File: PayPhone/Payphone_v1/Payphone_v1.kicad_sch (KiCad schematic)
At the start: 0 parts

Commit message: Payphone_v1: schematic started (MCP23008, relay, J1, U2 placed)
Co-Authored-By: Claude Sonnet 5.5 <noreply@anthropic.com>
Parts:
- added J1: JST_05, Connector_JST:JST_EH_B5B-EH-A_1x05_P2.50mm_Vertical, symbol PCM_SL_Connectors:JST_05
- added K1: G6S-2, symbol Relay:G6S-2
- added U1: MCP23008-xP, Package_DIP:DIP-18_W7.62mm, symbol Interface_Expansion:MCP23008-xP
- added U2: MC34063AP, Package_DIP:DIP-8_W7.62mm, symbol Regulator_Switching:MC34063AP

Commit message: Payphone_v1: all active parts, diodes, C_out, inductors, trimmer and connectors placed with footprints (no wires)
Co-Authored-By: Claude Sonnet 5.5 <noreply@anthropic.com>
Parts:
- added C1: 220uF/200V, Capacitor_THT:CP_Radial_D18.0mm_P7.50mm, symbol Device:C_Polarized
- added D1: 1N5819, Diode_THT:D_DO-41_SOD81_P10.16mm_Horizontal, symbol Diode:1N5819
- added D2: UF4003, Diode_THT:D_DO-41_SOD81_P10.16mm_Horizontal, symbol Custom:UF4003
- added D3: 1.5KE150A, Diode_THT:D_DO-201AD_P15.24mm_Horizontal, symbol Diode:1.5KExxA
- added D4: 1N4148, Diode_THT:D_DO-35_SOD27_P7.62mm_Horizontal, symbol Diode:1N4148
- added D5: 15V, Diode_THT:D_DO-41_SOD81_P10.16mm_Horizontal, symbol Device:D_Zener
- added D6: 12V, Diode_THT:D_DO-41_SOD81_P10.16mm_Horizontal, symbol Device:D_Zener
- added J2: Molex_26-60-4030, Connector_Molex:Molex_KK-396_A-41791-0003_1x03_P3.96mm_Vertical, symbol Connector:Conn_01x03_Pin
- added J3: Molex_26-60-4040, Connector_Molex:Molex_KK-396_A-41791-0004_1x04_P3.96mm_Vertical, symbol Connector:Conn_01x04_Pin
- added J4: HV_SELECT, Connector_PinHeader_2.54mm:PinHeader_1x04_P2.54mm_Vertical, symbol Connector:Conn_01x04_Pin
- added J5: SPARE_IO, Connector_PinHeader_2.54mm:PinHeader_1x04_P2.54mm_Vertical, symbol Connector:Conn_01x04_Pin
- added L1: 100uH, Inductor_THT:L_Radial_D10.0mm_P5.00mm_Fastron_07M, symbol Device:L
- added L2: 220uH, Inductor_THT:L_Radial_D10.0mm_P5.00mm_Fastron_07M, symbol Device:L
- added Q1, Q3: IRF630, Package_TO_SOT_THT:TO-220-3_Vertical, symbol Custom:IRF630
- added Q2, Q4, Q5: 2N7000, Package_TO_SOT_THT:TO-92_Inline, symbol Transistor_FET:2N7000
- added RV1: 10k, Potentiometer_THT:Potentiometer_Bourns_3296W_Vertical, symbol Device:R_Potentiometer_Trim
- added U3: UC3843AN, Package_DIP:DIP-8_W7.62mm, symbol Custom:UC3843AN

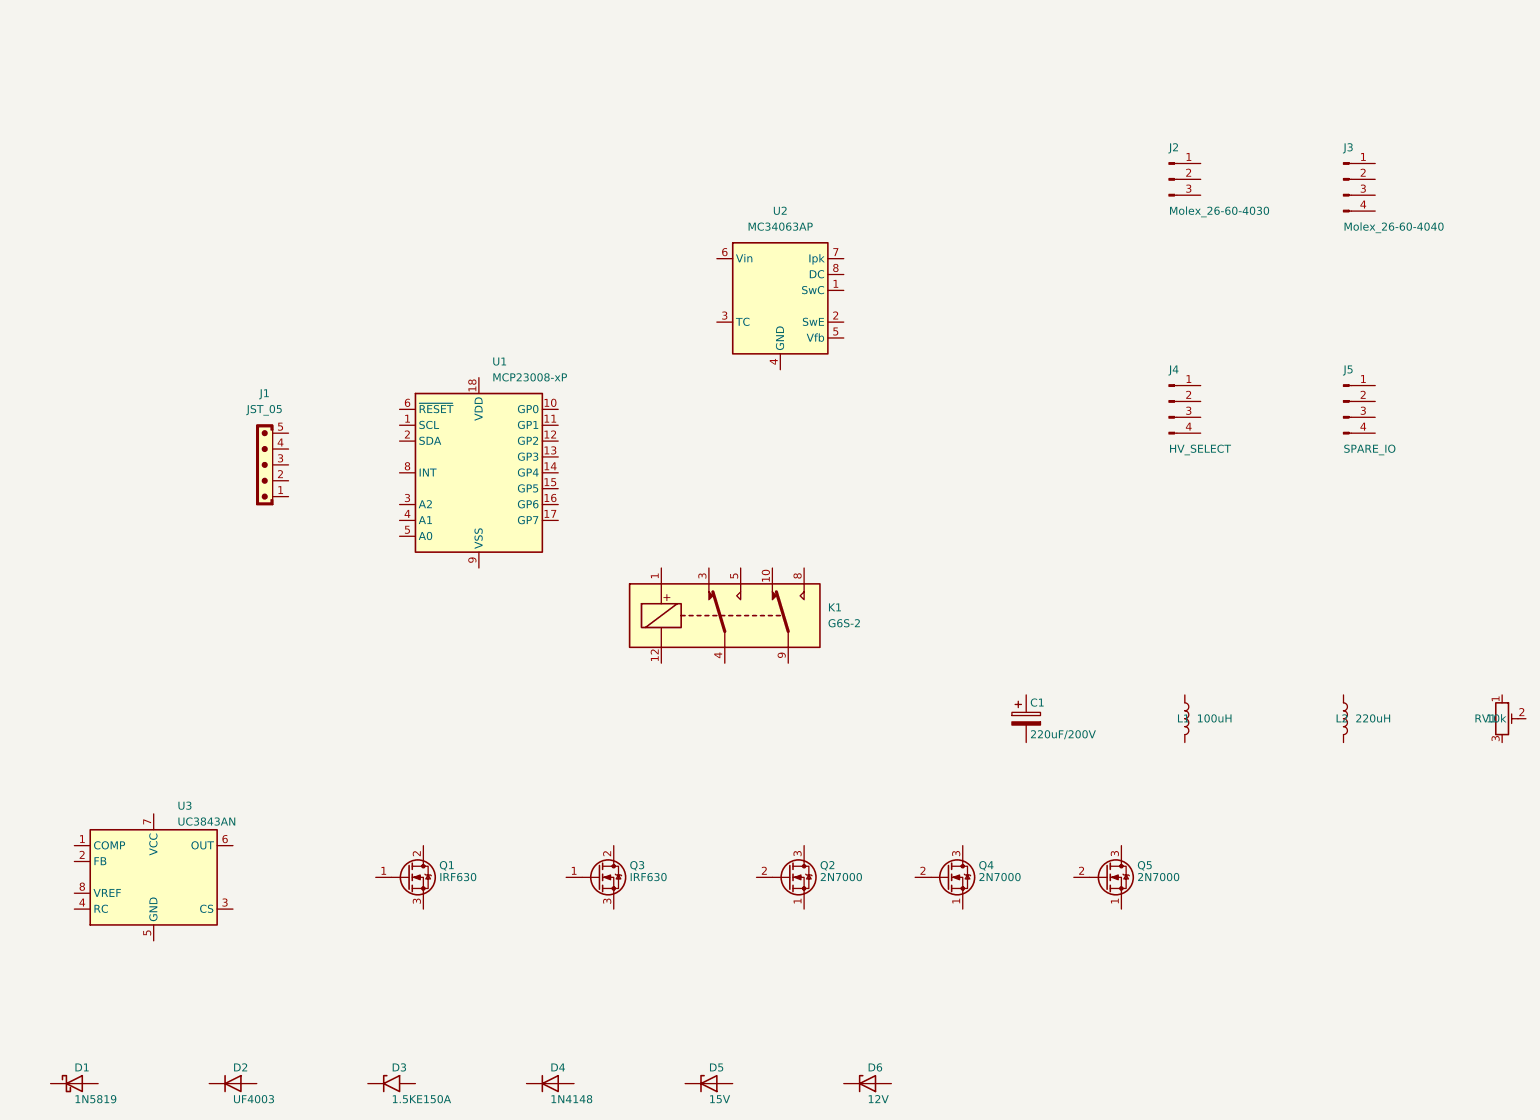
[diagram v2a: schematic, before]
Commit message: Bluetooth docs: 3-dash table separators so MacDown renders the tables
Co-Authored-By: Claude Sonnet 5.5 <noreply@anthropic.com>
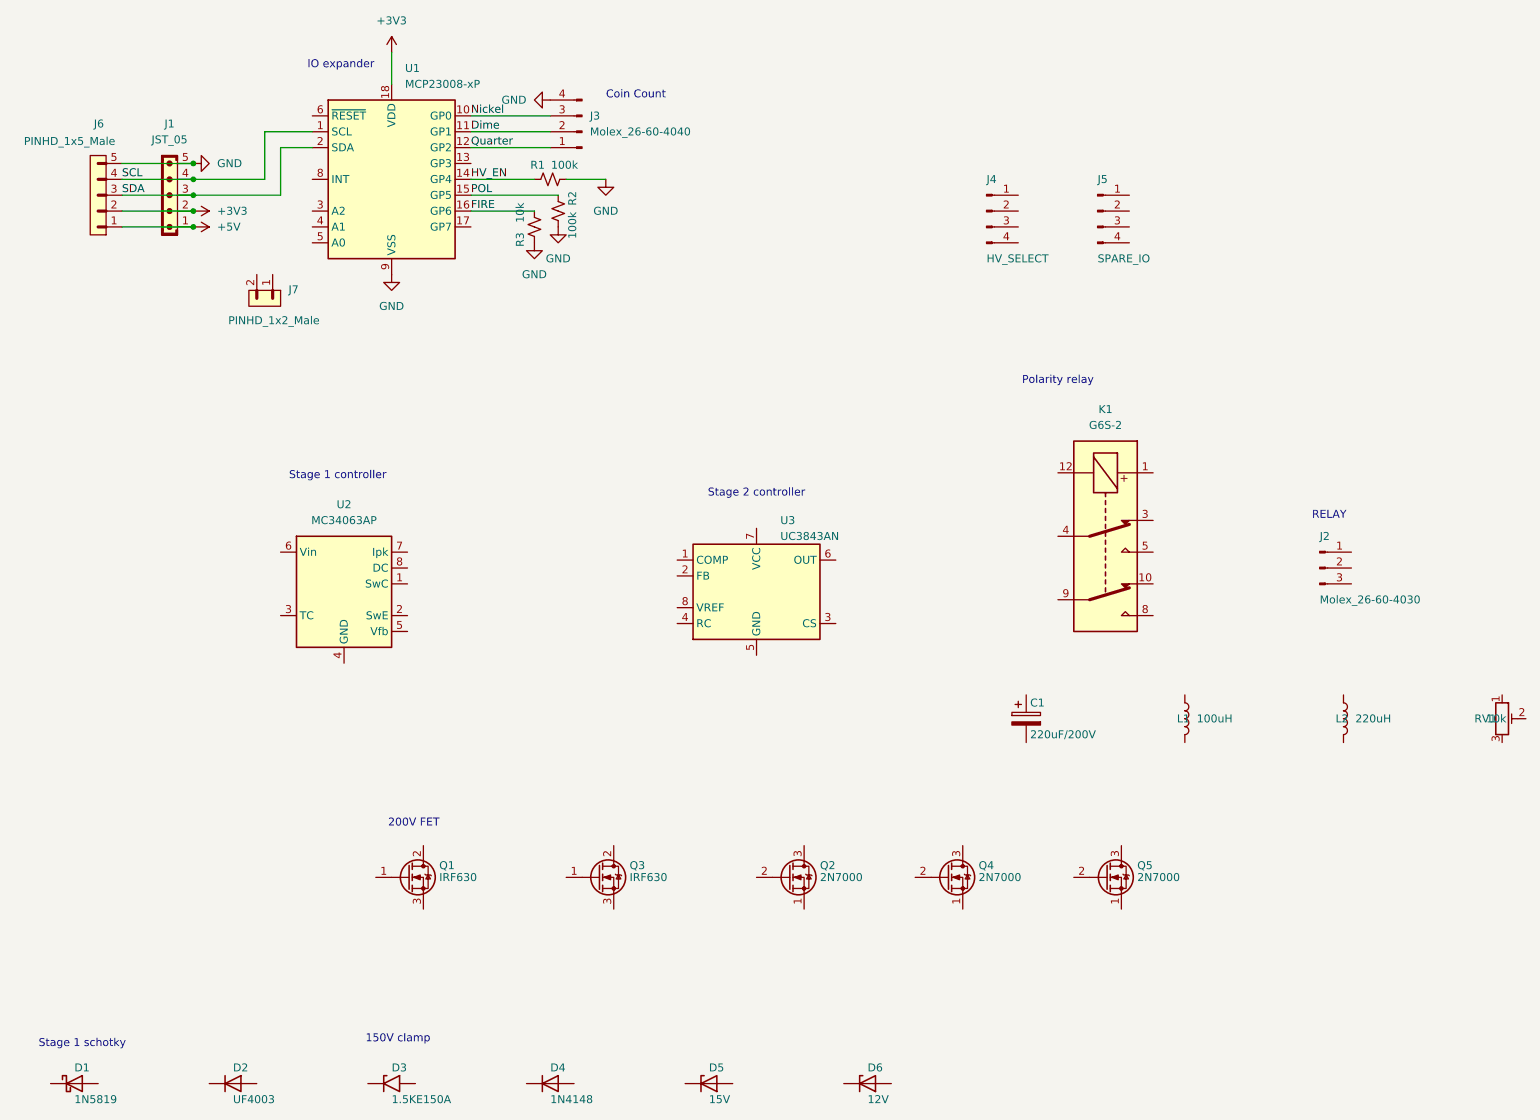
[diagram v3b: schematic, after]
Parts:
- added J6: PINHD_1x5_Male, Connector_PinHeader_2.54mm:PinHeader_1x05_P2.54mm_Vertical, symbol PCM_SL_Pin_Headers:PINHD_1x5_Male
- added J7: PINHD_1x2_Male, Connector_PinHeader_2.54mm:PinHeader_1x02_P2.54mm_Vertical, symbol PCM_SL_Pin_Headers:PINHD_1x2_Male
- added R1, R2: 100k, PCM_SparkFun-Resistor:R_0603_1608Metric, symbol PCM_SparkFun-Resistor:R_Small
- added R3: 10k, PCM_SparkFun-Resistor:R_0603_1608Metric, symbol PCM_SparkFun-Resistor:R_Small
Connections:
- net +5V: now reaches J1.1
- net +5V: now also J6.1
- net +3V3: now reaches J1.2
- net +3V3: now also U1.18 (VDD), J6.2
- net SDA: now reaches J1.3
- net SDA: now also U1.2 (SDA), J6.3
- net SCL: now reaches J1.4
- net SCL: now also U1.1 (SCL), J6.4
- net GND: now reaches J1.5
- net GND: now also J3.4 (Pin_4), U1.9 (VSS), J6.5, R1.1, R2.1, R3.2
- net Nickel: now reaches U1.10 (GP0)
- net Nickel: now also J3.3 (Pin_3)
- net Dime: now reaches U1.11 (GP1)
- net Dime: now also J3.2 (Pin_2)
- net Quarter: now reaches U1.12 (GP2)
- net Quarter: now also J3.1 (Pin_1)
- net HV_EN: now reaches U1.14 (GP4)
- net HV_EN: now also R1.2
- net POL: now reaches U1.15 (GP5)
- net POL: now also R2.2
- net FIRE: now reaches U1.16 (GP6)
- net FIRE: now also R3.1
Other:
- note added: "150V clamp"
- note added: "200V FET"
- note added: "Coin Count"
- note added: "IO expander"
- note added: "Polarity relay"
- note added: "RELAY"
- note added: "Stage 1 controller"
- note added: "Stage 1 schotky"
- note added: "Stage 2 controller"
- moved on the sheet: J1, J2, J3, J4, J5, K1, U1, U2, U3
